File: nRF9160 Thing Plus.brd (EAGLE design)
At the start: 58.4 x 22.9 mm, 127 parts, among them J1 USB Female C, J10 QWIIC_RIGHT_ANGLE, J2 CON-HEADER-1X12-MALE-PIN, J3 CON-HEADER-1X16-MALE-PIN, J4 CON-1909763-1, J6 CON-SIM-104224-0820, J7 CON-1909763-1, J8 CON-FTSH-105-XX-X-DV, Q1 MOSFET-P-SC89, Q2 MOSFET-DUAL-COMP-SOT563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

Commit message: SF Update
- Added PROD_ID info to new parts in temp libraries
- Moved new parts to temp libraries
- Added second fiducial to the top side of the board
- Rotated buzzard labels for GPIO 0/SDA and 1/SCL to match the other labels
- Shifted U9, R2, R7 to prevent overlap with reset label
- Removed date text on layer 22 (bPlace) and replaced with version text on bottom copper layer
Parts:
- removed U$25: (no value), buzzard_labels:0#SDA0
- added U$12: (no value), buzzard_labels:SCL#11
- added U$13: (no value), buzzard_labels:SDA#00
- J6: device wolff-den:MOLEX_104224-0820 -> nRF9160-Connectors:MOLEX_104224-0820
- J8: device wolff-den:SAMTEC_FTSH-105-XX-X-DV -> nRF9160-Connectors:SAMTEC_FTSH-105-XX-X-DV
- U$24: value (none) -> FIDUCIAL-1MM; device buzzard_labels-2:1#SCL0 -> wolff-den:FIDUCIAL-1MM
- U6: device wolff-den:WIN_ZP-8-L -> nRF9160-IC:WIN_ZP-8-L
- moved U$24 48.1 mm to (5.67, 1.50), flipped to the top, turned to 0 degrees
- moved U$35 16.4 mm to (53.2, 19.6)
- moved R7 0.76 mm to (8.98, 7.74)
- moved R2 0.63 mm to (10.4, 7.77)
- moved U9 0.51 mm to (12.4, 7.70)
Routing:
- net PS_EN_CC: track 4.83 -> 5.69 mm
- net MODE/WAKE: track 18.1 -> 18.6 mm
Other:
- board text added: "V1"
- board text removed: ">LAST_DATE_TIME"

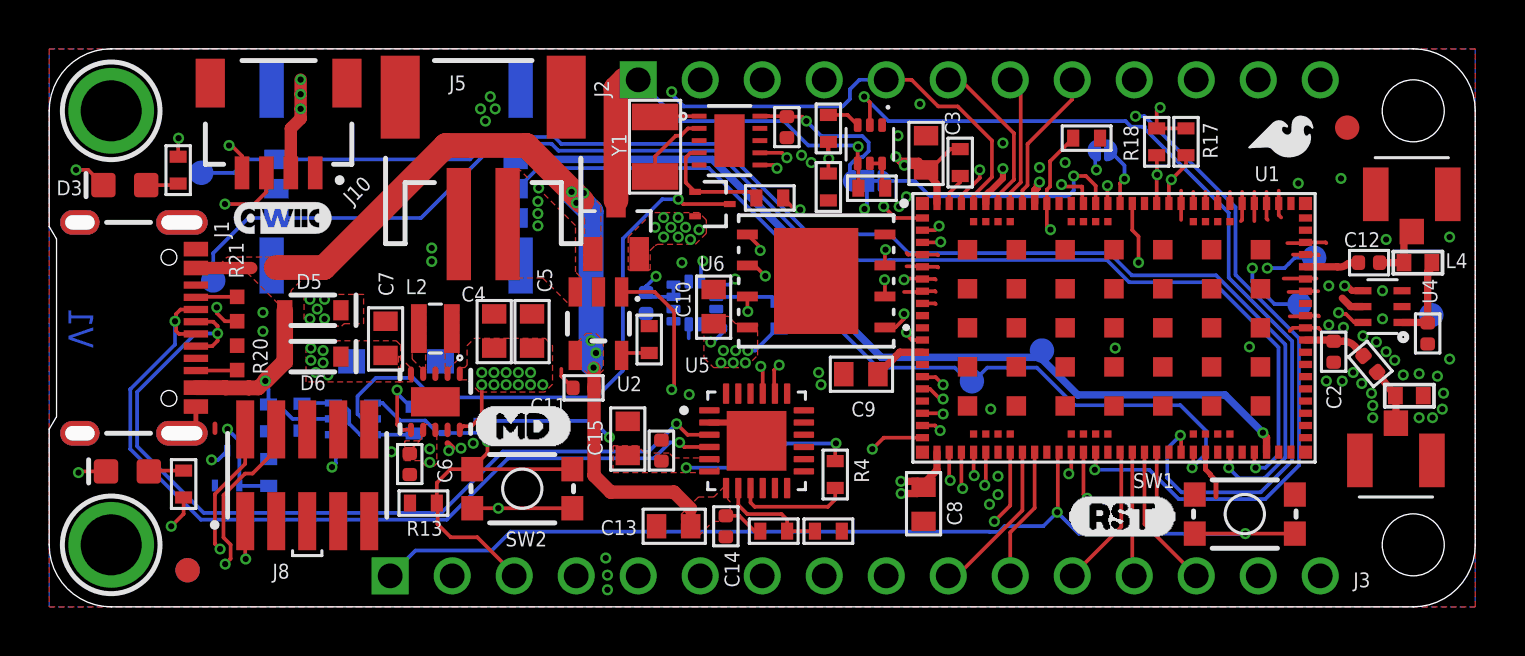
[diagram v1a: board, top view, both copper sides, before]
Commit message: Cleaned up silkscreen labels around U9, R2, R7 Fixed some of the text related to fab export drawings.
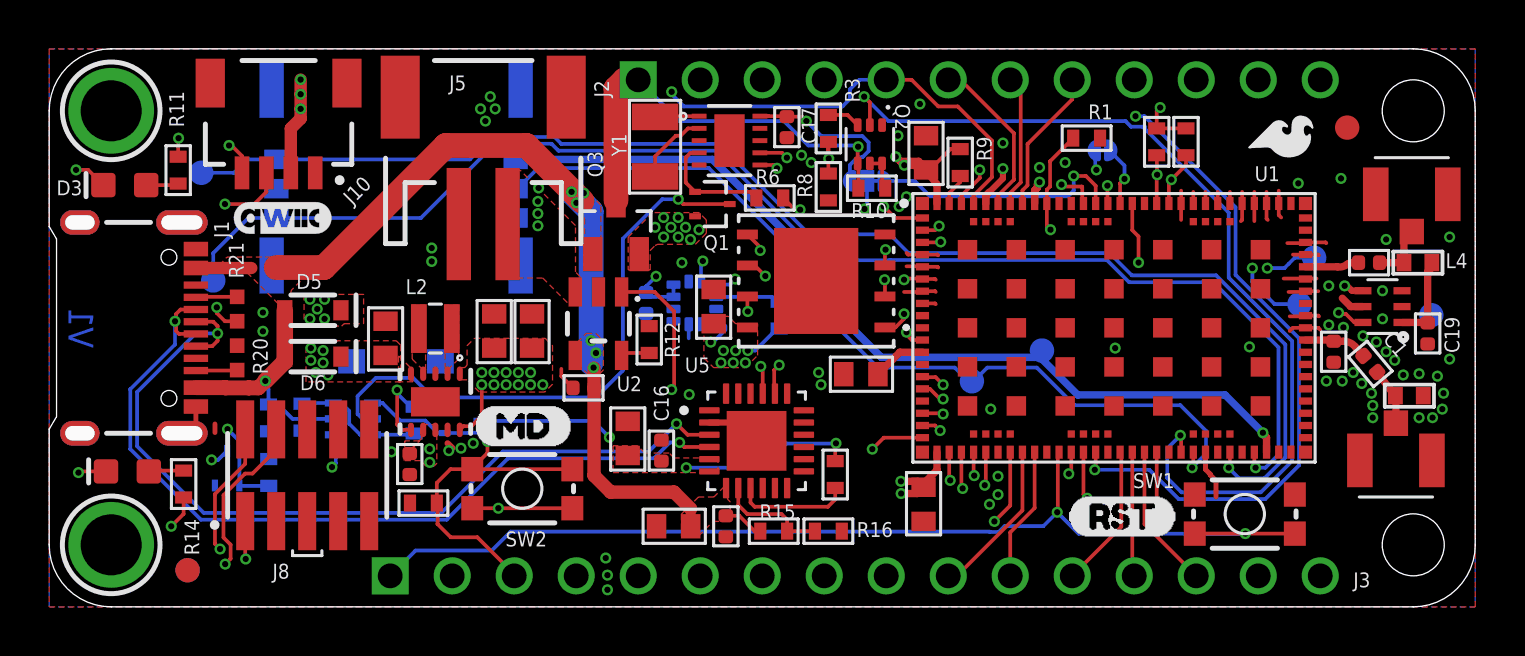
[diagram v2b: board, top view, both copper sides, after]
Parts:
- moved U$5 12.5 mm to (-164.7, -120.1)
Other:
- board text added: "Sparkfun"
- board text added: "nRF9160 Thing Plus"
- board text removed: "Confidential - Property of Circuit Dojo LLC"
- board text removed: "nRF9160 Featherwing"
